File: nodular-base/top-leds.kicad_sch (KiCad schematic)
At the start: 18 parts, among them SW1 SW_Push, SW2 SW_Push, SW3 SW_Push, SW4 SW_Push, SW5 SW_Push, SW6 SW_Push

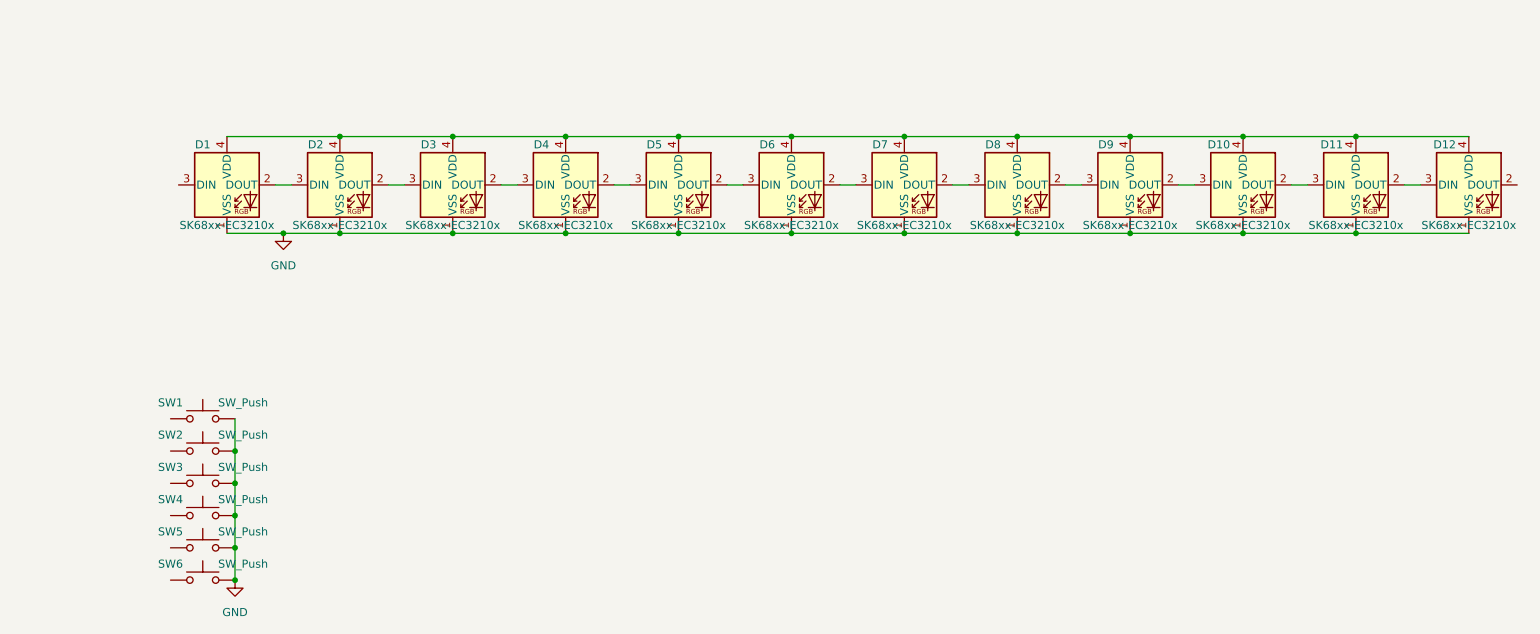
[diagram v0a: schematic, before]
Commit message: Update layout for top board, add library items
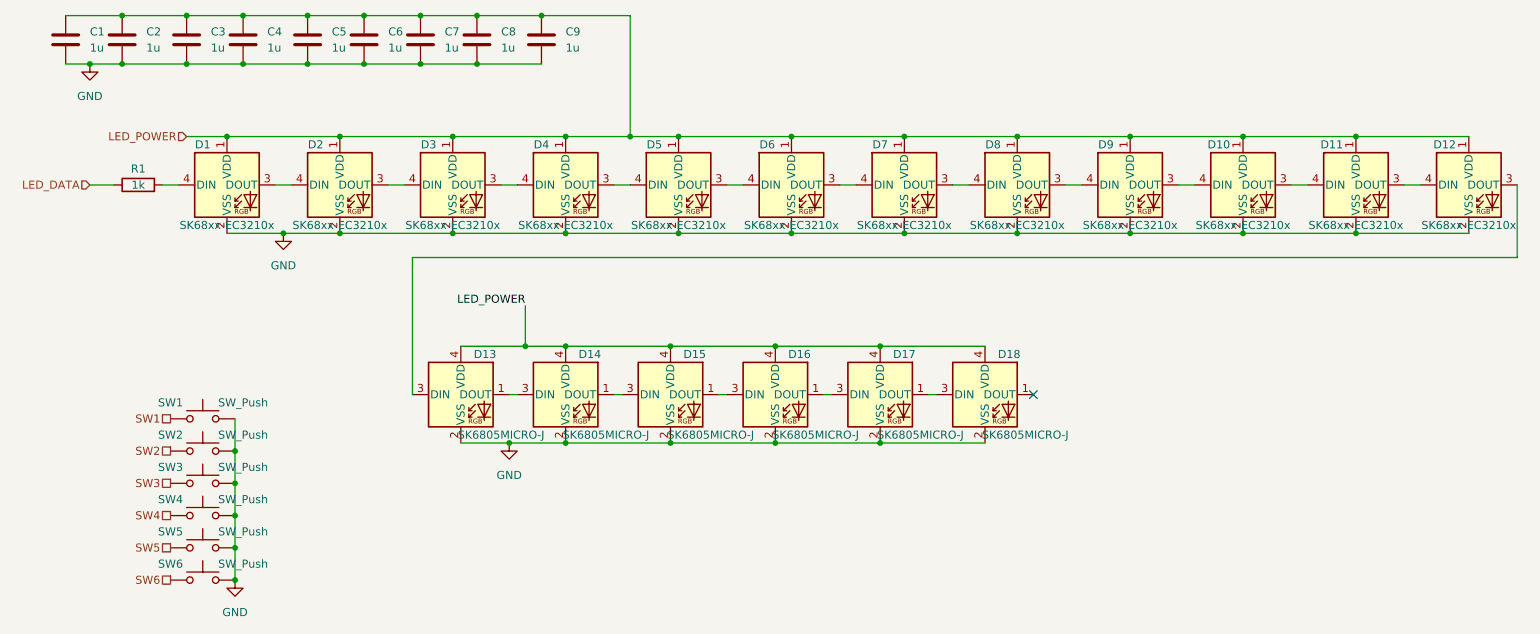
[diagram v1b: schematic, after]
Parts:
- added C1, C2, C3, C4, C5, C6, C7, C8, C9: 1u, Capacitor_SMD:C_0402_1005Metric, symbol Device:C
- added D13, D14, D15, D16, D17, D18: SK6805MICRO-J, LED_SMD:LED_SK6805_PLCC4_2.4x2.7mm_P1.3mm, symbol LED:SK6812MINI
- added R1: 1k, Resistor_SMD:R_0402_1005Metric, symbol Device:R
- D1, D10, D11, D12, D2, D3, D4, D5, D6, D7, D8, D9: footprint nodular:SK68XX-EC3210F -> nodular:SK6805SIDE-S; symbol nodular:SK68xx-EC3210x -> nodular:SK6805SIDE-S
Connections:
- net GND: now also D1.2 (VSS), D10.2 (VSS), D11.2 (VSS), D12.2 (VSS), D2.2 (VSS), D3.2 (VSS), D4.2 (VSS), D5.2 (VSS), D6.2 (VSS), D7.2 (VSS), D8.2 (VSS), D9.2 (VSS), C1.2, C2.2, C3.2, C4.2, C5.2, C6.2, C7.2, C8.2, C9.2, D13.2 (VSS), D14.2 (VSS), D15.2 (VSS), D16.2 (VSS), D17.2 (VSS), D18.2 (VSS); no longer D1.1 (VSS), D10.1 (VSS), D11.1 (VSS), D12.1 (VSS), D2.1 (VSS), D3.1 (VSS), D4.1 (VSS), D5.1 (VSS), D6.1 (VSS), D7.1 (VSS), D8.1 (VSS), D9.1 (VSS)
- net at D2.3 (DOUT): now also D3.4 (DIN); no longer D1.2 (DOUT)
- net at D1.3 (DOUT): now also D2.4 (DIN)
- net SW1: now reaches SW1.1
- net at D3.3 (DOUT): now also D4.4 (DIN); no longer D2.2 (DOUT)
- net SW5: now reaches SW5.1
- net at D11.3 (DOUT): now also D12.4 (DIN); no longer D10.2 (DOUT)
- net at D10.3 (DOUT): now also D11.4 (DIN); no longer D9.2 (DOUT)
- net at D5.3 (DOUT): now also D6.4 (DIN); no longer D4.2 (DOUT)
- net at D4.3 (DOUT): now also D5.4 (DIN); no longer D3.2 (DOUT)
- net SW2: now reaches SW2.1
- net at D12.3 (DOUT): now also D13.3 (DIN); no longer D11.2 (DOUT)
- net at D6.3 (DOUT): now also D7.4 (DIN); no longer D5.2 (DOUT)
- net at D7.3 (DOUT): now also D8.4 (DIN); no longer D6.2 (DOUT)
- net at D9.3 (DOUT): now also D10.4 (DIN); no longer D8.2 (DOUT)
- net at D8.3 (DOUT): now also D9.4 (DIN); no longer D7.2 (DOUT)
- net SW4: now reaches SW4.1
- net SW6: now reaches SW6.1
- net SW3: now reaches SW3.1
- new net: D1.4 (DIN), R1.2
- new net: D14.1 (DOUT), D15.3 (DIN)
- new net: D13.1 (DOUT), D14.3 (DIN)
- new net: D15.1 (DOUT), D16.3 (DIN)
- new net: D17.1 (DOUT), D18.3 (DIN)
- new net: D16.1 (DOUT), D17.3 (DIN)
- new net LED_DATA: R1.1
- new net LED_POWER: C1.1, C2.1, C3.1, C4.1, C5.1, C6.1, C7.1, C8.1, C9.1, D1.1 (VDD), D10.1 (VDD), D11.1 (VDD), D12.1 (VDD), D13.4 (VDD), D14.4 (VDD), D15.4 (VDD), D16.4 (VDD), D17.4 (VDD), D18.4 (VDD), D2.1 (VDD), D3.1 (VDD), D4.1 (VDD), D5.1 (VDD), D6.1 (VDD), D7.1 (VDD), D8.1 (VDD), D9.1 (VDD)
- no-connect marks 0 -> 1

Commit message: Add 3d models and fix erc errors
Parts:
- D13, D14, D15, D16, D17, D18: footprint LED_SMD:LED_SK6805_PLCC4_2.4x2.7mm_P1.3mm -> nodular:LED_SK6805_PLCC4_2.4x2.7mm_P1.3mm
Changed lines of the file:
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@@
       (effects (font (size 1.27 1.27)))
     )
-    (property "Footprint" "LED_SMD:LED_SK6805_PLCC4_2.4x2.7mm_P1.3mm" (at 104.14 90.17 0)
+    (property "Footprint" "nodular:LED_SK6805_PLCC4_2.4x2.7mm_P1.3mm" (at 104.14 90.17 0)
       (effects (font (size 1.27 1.27)) (justify left top) hide)
     )
@@
       (effects (font (size 1.27 1.27)))
     )
-    (property "Footprint" "LED_SMD:LED_SK6805_PLCC4_2.4x2.7mm_P1.3mm" (at 120.65 90.17 0)
+    (property "Footprint" "nodular:LED_SK6805_PLCC4_2.4x2.7mm_P1.3mm" (at 120.65 90.17 0)
       (effects (font (size 1.27 1.27)) (justify left top) hide)
     )
@@
       (effects (font (size 1.27 1.27)))
     )
-    (property "Footprint" "LED_SMD:LED_SK6805_PLCC4_2.4x2.7mm_P1.3mm" (at 170.18 90.17 0)
+    (property "Footprint" "nodular:LED_SK6805_PLCC4_2.4x2.7mm_P1.3mm" (at 170.18 90.17 0)
       (effects (font (size 1.27 1.27)) (justify left top) hide)
     )
@@
       (effects (font (size 1.27 1.27)))
     )
-    (property "Footprint" "LED_SMD:LED_SK6805_PLCC4_2.4x2.7mm_P1.3mm" (at 137.16 90.17 0)
+    (property "Footprint" "nodular:LED_SK6805_PLCC4_2.4x2.7mm_P1.3mm" (at 137.16 90.17 0)
       (effects (font (size 1.27 1.27)) (justify left top) hide)
     )
@@
       (effects (font (size 1.27 1.27)))
     )
-    (property "Footprint" "LED_SMD:LED_SK6805_PLCC4_2.4x2.7mm_P1.3mm" (at 87.63 90.17 0)
+    (property "Footprint" "nodular:LED_SK6805_PLCC4_2.4x2.7mm_P1.3mm" (at 87.63 90.17 0)
       (effects (font (size 1.27 1.27)) (justify left top) hide)
     )
@@
       (effects (font (size 1.27 1.27)))
     )
-    (property "Footprint" "LED_SMD:LED_SK6805_PLCC4_2.4x2.7mm_P1.3mm" (at 153.67 90.17 0)
-      (effects (font (size 1.27 1.27)) (justify left top) hide)
-    )
+    (property "Footprint" "nodular:LED_SK6805_PLCC4_2.4x2.7mm_P1.3mm" (at 153.67 90.17 0)
+      (effects (font (size 1.27 1.27)) (justify left top) hide)
+    )
